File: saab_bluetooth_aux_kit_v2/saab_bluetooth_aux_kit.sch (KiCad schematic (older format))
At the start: 11 parts, among them J1 Barrel_Jack, U1 MCP1703A-5002_SOT223, U2 ESP32-WROOM-30GPIO, U3 MCP2515-xST, U4 UDA1334A_BREAKOUT, U5 MCP2551-I-P, Y1 Crystal

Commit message: Working on new bluetooth+can module from scratch
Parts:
- removed U4: UDA1334A_BREAKOUT, custom_footprints:UDA1334A-Breakout, symbol custom_symbols:UDA1334A_BREAKOUT
- C1, C2: footprint (none) -> Capacitor_SMD:C_0805_2012Metric_Pad1.15x1.40mm_HandSolder
- R1, R2: footprint (none) -> Resistor_SMD:R_0805_2012Metric_Pad1.15x1.40mm_HandSolder
- Y1: footprint (none) -> Crystal:Crystal_SMD_SeikoEpson_MA505-2Pin_12.7x5.1mm
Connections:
- net labels added: VIN_12V
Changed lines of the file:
@@
 $Descr A4 11693 8268
 encoding utf-8
-Sheet 1 1
+Sheet 1 2
 Title ""
 Date ""
@@
 F 3 "" H 5100 4550 118 0001 C CNN
 	1    5100 4550
-	1    0    0    -1
-$EndComp
-$Comp
-L custom_symbols:UDA1334A_BREAKOUT U4
-U 1 1 5EA5F0CB
-P 7200 5500
-F 0 "U4" H 7878 5546 50  0000 L CNN
-F 1 "UDA1334A_BREAKOUT" H 7878 5455 50  0000 L CNN
-F 2 "custom_footprints:UDA1334A-Breakout" H 7200 5500 50  0001 C CNN
-F 3 "" H 7200 5500 50  0001 C CNN
-	1    7200 5500
 	1    0    0    -1
 $EndComp
@@
 Text GLabel 8150 1250 0    50   Input ~ 0
 SPI_MOSI
-Text GLabel 6800 5950 3    50   Input ~ 10
-3VDC
-Text GLabel 7000 5950 3    50   Input ~ 10
-GND
-Text GLabel 7100 5950 3    50   Input ~ 0
+Text GLabel 7300 5050 0    50   Input ~ 10
+GND
+Text GLabel 7300 3700 0    50   Input ~ 0
 I2S_WSEL
 Text GLabel 4300 4400 0    50   Input ~ 0
 I2S_WSEL
-Text GLabel 7200 5950 3    50   Input ~ 0
+Text GLabel 7300 3800 0    50   Input ~ 0
 I2S_DIN
 Text GLabel 5850 3800 2    50   Input ~ 0
 I2S_DIN
-Text GLabel 7300 5950 3    50   Input ~ 0
+Text GLabel 7300 3600 0    50   Input ~ 0
 I2S_BCLK
 Text GLabel 4300 4500 0    50   Input ~ 0
 I2S_BCLK
-Text GLabel 7050 5050 1    50   Input ~ 10
-GND
-Text GLabel 7250 5050 1    50   Input ~ 10
+Text GLabel 7300 4300 0    50   Input ~ 10
+GND
+Text GLabel 7300 4400 0    50   Input ~ 10
 GND
 $Comp
@@
 F 0 "R2" H 9859 2296 50  0000 L CNN
 F 1 "10k" H 9859 2205 50  0000 L CNN
-F 2 "" H 9800 2250 50  0001 C CNN
+F 2 "Resistor_SMD:R_0805_2012Metric_Pad1.15x1.40mm_HandSolder" H 9800 2250 50  0001 C CNN
 F 3 "~" H 9800 2250 50  0001 C CNN
 	1    9800 2250
@@
 F 0 "R1" H 9409 2596 50  0000 L CNN
 F 1 "10k" H 9409 2505 50  0000 L CNN
-F 2 "" H 9350 2550 50  0001 C CNN
+F 2 "Resistor_SMD:R_0805_2012Metric_Pad1.15x1.40mm_HandSolder" H 9350 2550 50  0001 C CNN
 F 3 "~" H 9350 2550 50  0001 C CNN
 	1    9350 2550
@@
 F 0 "Y1" V 7104 2231 50  0000 L CNN
 F 1 "Crystal" V 7195 2231 50  0000 L CNN
-F 2 "" H 7150 2100 50  0001 C CNN
+F 2 "Crystal:Crystal_SMD_SeikoEpson_MA505-2Pin_12.7x5.1mm" H 7150 2100 50  0001 C CNN
 F 3 "~" H 7150 2100 50  0001 C CNN
 	1    7150 2100
 	0    1    1    0
 $EndComp
+$Comp
+L Device:C_Small C2
+U 1 1 5ED7C91E
+P 6850 2250
+F 0 "C2" V 6621 2250 50  0000 C CNN
+F 1 "27pF" V 6712 2250 50  0000 C CNN
+F 2 "Capacitor_SMD:C_0805_2012Metric_Pad1.15x1.40mm_HandSolder" H 6850 2250 50  0001 C CNN
+F 3 "~" H 6850 2250 50  0001 C CNN
+	1    6850 2250
+	0    1    1    0
+$EndComp
+Wire Wire Line
+	6950 1950 7150 1950
+Wire Wire Line
+	7150 2250 6950 2250
+Wire Wire Line
+	6750 1950 6700 1950
+Wire Wire Line
+	6700 1950 6700 2100
+Wire Wire Line
+	6700 2250 6750 2250
+Wire Wire Line
+	6700 2100 6650 2100
+Connection ~ 6700 2100
+Wire Wire Line
+	6700 2100 6700 2250
+Text GLabel 6650 2100 0    50   Input ~ 10
+GND
+Wire Wire Line
+	7450 2050 7450 1950
+Wire Wire Line
+	7450 1950 7150 1950
+Wire Wire Line
+	7450 2050 8150 2050
+Connection ~ 7150 1950
+Wire Wire Line
+	7150 2250 7600 2250
+Wire Wire Line
+	7600 2250 7600 2150
+Wire Wire Line
+	7600 2150 8150 2150
+Connection ~ 7150 2250
+Wire Notes Line
+	6350 750  10900 750
+Wire Notes Line
+	10900 750  10900 2800
+Wire Notes Line
+	10900 2800 6350 2800
+Wire Notes Line
+	6350 2800 6350 750
+Text Notes 6400 850  0    50   ~ 0
+CAN INTERFACE
+$Sheet
+S 7300 3450 2000 1700
+U 5EE7716E
+F0 "UDA1334 I2S" 50
+F1 "uda1334_submodule.sch" 50
+F2 "BCK" I L 7300 3600 50
+F3 "WS" I L 7300 3700 50
+F4 "DATAIN" I L 7300 3800 50
+F5 "PLL0" I L 7300 3900 50
+F6 "SYSCLK_IN" I L 7300 4000 50
+F7 "DEEM" I L 7300 4100 50
+F8 "MUTE" I L 7300 4200 50
+F9 "SFOR0" I L 7300 4300 50
+F10 "SFOR1" I L 7300 4400 50
+F11 "GND" I L 7300 5050 50
+F12 "VIN" I L 7300 4950 50
+$EndSheet
+Text GLabel 7300 4950 0    50   Input ~ 10
+VIN_12V
+Text GLabel 2150 2050 1    50   Input ~ 10
+VIN_12V
 $Comp
 L Device:C_Small C1
@@
 F 0 "C1" V 6621 1950 50  0000 C CNN
 F 1 "27pF" V 6712 1950 50  0000 C CNN
-F 2 "" H 6850 1950 50  0001 C CNN
+F 2 "Capacitor_SMD:C_0805_2012Metric_Pad1.15x1.40mm_HandSolder" H 6850 1950 50  0001 C CNN
 F 3 "~" H 6850 1950 50  0001 C CNN
 	1    6850 1950
 	0    1    1    0
 $EndComp
-$Comp
-L Device:C_Small C2
-U 1 1 5ED7C91E
-P 6850 2250
-F 0 "C2" V 6621 2250 50  0000 C CNN
-F 1 "27pF" V 6712 2250 50  0000 C CNN
-F 2 "" H 6850 2250 50  0001 C CNN
-F 3 "~" H 6850 2250 50  0001 C CNN
-	1    6850 2250
-	0    1    1    0
-$EndComp
-Wire Wire Line
-	6950 1950 7150 1950
-Wire Wire Line
-	7150 2250 6950 2250
-Wire Wire Line
-	6750 1950 6700 1950
-Wire Wire Line
-	6700 1950 6700 2100
-Wire Wire Line
-	6700 2250 6750 2250
-Wire Wire Line
-	6700 2100 6650 2100
-Connection ~ 6700 2100
-Wire Wire Line
-	6700 2100 6700 2250
-Text GLabel 6650 2100 0    50   Input ~ 10
-GND
-Wire Wire Line
-	7450 2050 7450 1950
-Wire Wire Line
-	7450 1950 7150 1950
-Wire Wire Line
-	7450 2050 8150 2050
-Connection ~ 7150 1950
-Wire Wire Line
-	7150 2250 7600 2250
-Wire Wire Line
-	7600 2250 7600 2150
-Wire Wire Line
-	7600 2150 8150 2150
-Connection ~ 7150 2250
-Wire Notes Line
-	6350 750  10900 750
-Wire Notes Line
-	10900 750  10900 2800
-Wire Notes Line
-	10900 2800 6350 2800
-Wire Notes Line
-	6350 2800 6350 750
-Text Notes 6400 850  0    50   ~ 0
-CAN INTERFACE
 $EndSCHEMATC

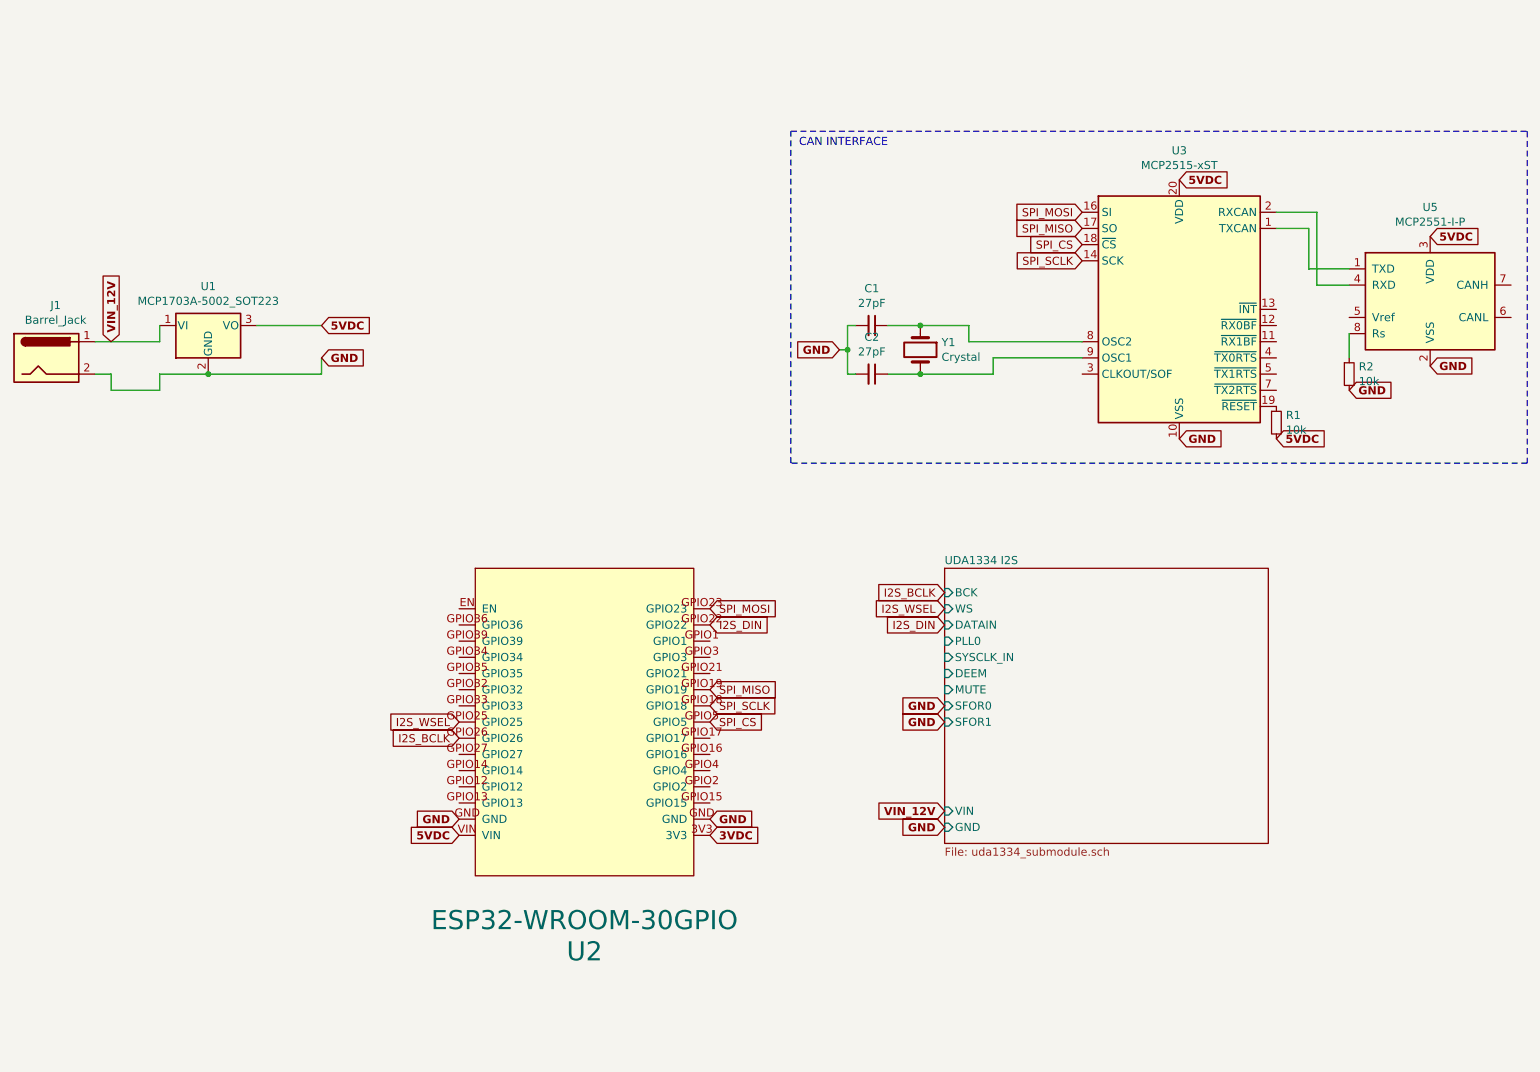
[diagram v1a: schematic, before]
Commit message: Experimenting with newer DAC chips
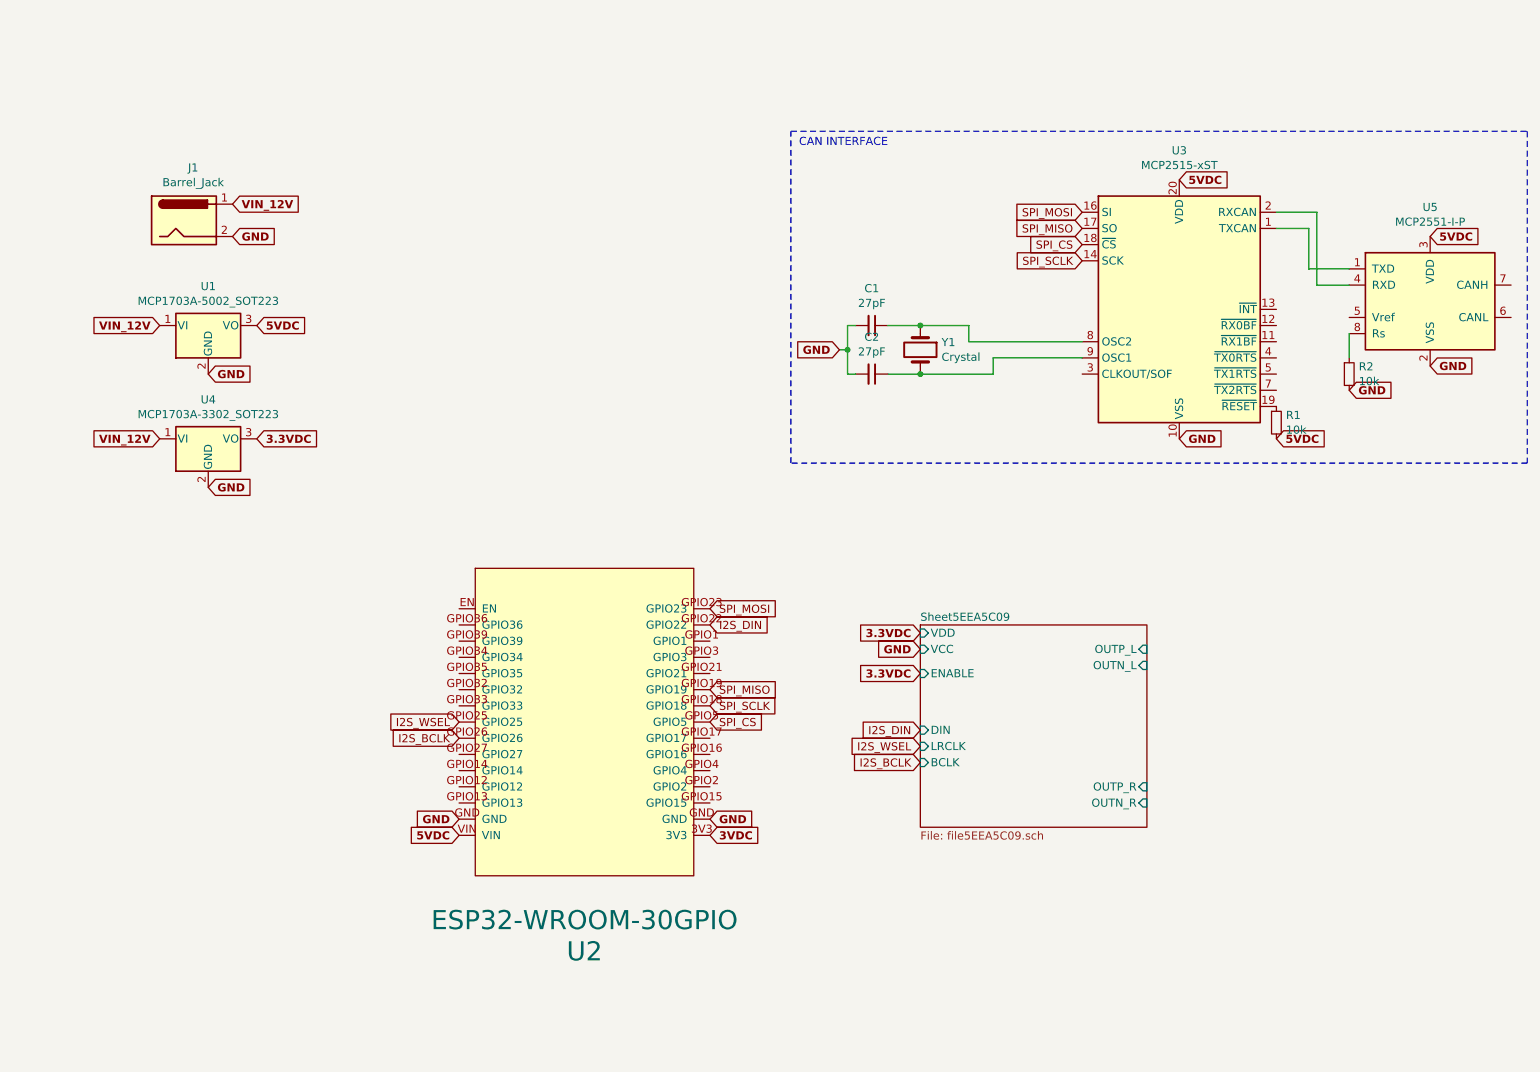
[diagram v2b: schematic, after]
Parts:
- added U4: MCP1703A-3302_SOT223, Package_TO_SOT_SMD:SOT-223-3_TabPin2, symbol Regulator_Linear:MCP1703A-3302_SOT223
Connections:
- net GND: now also U4.2 (GND)
- net VIN_12V: now also U4.1 (VI)
- new net 3.3VDC: U4.3 (VO)
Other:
- moved on the sheet: J1
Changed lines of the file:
@@
 	1    0    0    -1
 $EndComp
-Text GLabel 3450 1950 2    50   Input ~ 10
-5VDC
-Text GLabel 3450 2150 2    50   Input ~ 10
+Text GLabel 3050 1950 2    50   Input ~ 10
+5VDC
+Text GLabel 2750 2250 2    50   Input ~ 10
 GND
 Text GLabel 4300 5000 0    50   Input ~ 10
@@
 Text GLabel 8150 1250 0    50   Input ~ 0
 SPI_MOSI
-Text GLabel 7300 5050 0    50   Input ~ 10
-GND
-Text GLabel 7300 3700 0    50   Input ~ 0
-I2S_WSEL
 Text GLabel 4300 4400 0    50   Input ~ 0
 I2S_WSEL
-Text GLabel 7300 3800 0    50   Input ~ 0
-I2S_DIN
 Text GLabel 5850 3800 2    50   Input ~ 0
 I2S_DIN
-Text GLabel 7300 3600 0    50   Input ~ 0
-I2S_BCLK
 Text GLabel 4300 4500 0    50   Input ~ 0
 I2S_BCLK
-Text GLabel 7300 4300 0    50   Input ~ 10
-GND
-Text GLabel 7300 4400 0    50   Input ~ 10
-GND
 $Comp
 L Connector:Barrel_Jack J1
 U 1 1 5EB35333
-P 1750 2150
-F 0 "J1" H 1807 2475 50  0000 C CNN
-F 1 "Barrel_Jack" H 1807 2384 50  0000 C CNN
-F 2 "Connector_BarrelJack:BarrelJack_Wuerth_6941xx301002" H 1800 2110 50  0001 C CNN
-F 3 "~" H 1800 2110 50  0001 C CNN
-	1    1750 2150
-	1    0    0    -1
-$EndComp
-Wire Wire Line
-	2050 2050 2450 2050
-Wire Wire Line
-	2450 2050 2450 1950
-Wire Wire Line
-	2050 2250 2150 2250
-Wire Wire Line
-	2150 2250 2150 2350
-Wire Wire Line
-	2150 2350 2450 2350
-Wire Wire Line
-	2450 2250 2450 2350
-Wire Wire Line
-	3450 2250 3450 2150
-Wire Wire Line
-	3050 1950 3450 1950
-Wire Wire Line
-	2450 2250 2750 2250
+P 2600 1300
+F 0 "J1" H 2657 1625 50  0000 C CNN
+F 1 "Barrel_Jack" H 2657 1534 50  0000 C CNN
+F 2 "Connector_BarrelJack:BarrelJack_Wuerth_6941xx301002" H 2650 1260 50  0001 C CNN
+F 3 "~" H 2650 1260 50  0001 C CNN
+	1    2600 1300
+	1    0    0    -1
+$EndComp
 $Comp
 L Regulator_Linear:MCP1703A-5002_SOT223 U1
@@
 	1    0    0    -1
 $EndComp
-Connection ~ 2750 2250
-Wire Wire Line
-	2750 2250 3450 2250
 $Comp
 L Interface_CAN_LIN:MCP2515-xST U3
@@
 Text Notes 6400 850  0    50   ~ 0
 CAN INTERFACE
-$Sheet
-S 7300 3450 2000 1700
-U 5EE7716E
-F0 "UDA1334 I2S" 50
-F1 "uda1334_submodule.sch" 50
-F2 "BCK" I L 7300 3600 50
-F3 "WS" I L 7300 3700 50
-F4 "DATAIN" I L 7300 3800 50
-F5 "PLL0" I L 7300 3900 50
-F6 "SYSCLK_IN" I L 7300 4000 50
-F7 "DEEM" I L 7300 4100 50
-F8 "MUTE" I L 7300 4200 50
-F9 "SFOR0" I L 7300 4300 50
-F10 "SFOR1" I L 7300 4400 50
-F11 "GND" I L 7300 5050 50
-F12 "VIN" I L 7300 4950 50
-$EndSheet
-Text GLabel 7300 4950 0    50   Input ~ 10
-VIN_12V
-Text GLabel 2150 2050 1    50   Input ~ 10
-VIN_12V
 $Comp
 L Device:C_Small C1
@@
 	0    1    1    0
 $EndComp
+$Sheet
+S 7150 3800 1400 1250
+U 5EEA5C0A
+F0 "Sheet5EEA5C09" 50
+F1 "file5EEA5C09.sch" 50
+F2 "VCC" I L 7150 3950 50
+F3 "VDD" I L 7150 3850 50
+F4 "ENABLE" I L 7150 4100 50
+F5 "BCLK" I L 7150 4650 50
+F6 "LRCLK" I L 7150 4550 50
+F7 "OUTP_L" I R 8550 3950 50
+F8 "OUTN_L" I R 8550 4050 50
+F9 "OUTN_R" I R 8550 4900 50
+F10 "OUTP_R" I R 8550 4800 50
+F11 "DIN" I L 7150 4450 50
+$EndSheet
+Text GLabel 7150 4550 0    50   Input ~ 0
+I2S_WSEL
+Text GLabel 7150 4450 0    50   Input ~ 0
+I2S_DIN
+Text GLabel 7150 4650 0    50   Input ~ 0
+I2S_BCLK
+$Comp
+L Regulator_Linear:MCP1703A-3302_SOT223 U4
+U 1 1 5EED9837
+P 2750 2650
+F 0 "U4" H 2750 2892 50  0000 C CNN
+F 1 "MCP1703A-3302_SOT223" H 2750 2801 50  0000 C CNN
+F 2 "Package_TO_SOT_SMD:SOT-223-3_TabPin2" H 2750 2850 50  0001 C CNN
+F 3 "http://ww1.microchip.com/downloads/en/DeviceDoc/20005122B.pdf" H 2750 2600 50  0001 C CNN
+	1    2750 2650
+	1    0    0    -1
+$EndComp
+Text GLabel 2900 1400 2    50   Input ~ 10
+GND
+Text GLabel 2900 1200 2    50   Input ~ 10
+VIN_12V
+Text GLabel 2450 1950 0    50   Input ~ 10
+VIN_12V
+Text GLabel 2450 2650 0    50   Input ~ 10
+VIN_12V
+Text GLabel 2750 2950 2    50   Input ~ 10
+GND
+Text GLabel 3050 2650 2    50   Input ~ 10
+3.3VDC
+Text GLabel 7150 3850 0    50   Input ~ 10
+3.3VDC
+Text GLabel 7150 3950 0    50   Input ~ 10
+GND
+Text GLabel 7150 4100 0    50   Input ~ 10
+3.3VDC
 $EndSCHEMATC
